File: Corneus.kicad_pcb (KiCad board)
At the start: 2 copper layers, 0 parts

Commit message: PCB layout setup
imported JLCPCB design rules from sethhillbrand, set some settings per ai03's guide, about to import everything and start doing layout
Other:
- copper layers 2 -> 4
- net class Default: clearance 0.2 -> 0.254; trace_width 0.25 -> 0.254
- rule pad_to_mask_clearance: 0.05 -> 0
- rule trace_clearance: 0.2 -> 0.254
- rule trace_min: 0.2 -> 0.127
- rule via_min_size: 0.4 -> 0.6
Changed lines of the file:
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@@
 (kicad_pcb (version 20171130) (host pcbnew "(5.1.6)-1")
   (general
-    (thickness 1.6)
+    (thickness 1.6002)
     (drawings 0)
     (tracks 0)
@@
   )
   (layers
-    (0 F.Cu signal)
-    (31 B.Cu signal)
-    (32 B.Adhes user)
-    (33 F.Adhes user)
+    (0 Front signal)
+    (1 In1.Cu signal)
+    (2 In2.Cu signal)
+    (31 Back signal)
     (34 B.Paste user)
     (35 F.Paste user)
@@
     (38 B.Mask user)
     (39 F.Mask user)
-    (40 Dwgs.User user)
-    (41 Cmts.User user)
-    (42 Eco1.User user)
-    (43 Eco2.User user)
     (44 Edge.Cuts user)
     (45 Margin user)
     (46 B.CrtYd user)
     (47 F.CrtYd user)
-    (48 B.Fab user)
     (49 F.Fab user)
   )
   (setup
-    (last_trace_width 0.25)
-    (trace_clearance 0.2)
+    (last_trace_width 0.254)
+    (user_trace_width 0.15)
+    (user_trace_width 0.2)
+    (user_trace_width 0.4)
+    (user_trace_width 0.6)
+    (trace_clearance 0.254)
     (zone_clearance 0.508)
     (zone_45_only no)
-    (trace_min 0.2)
+    (trace_min 0.127)
     (via_size 0.8)
     (via_drill 0.4)
-    (via_min_size 0.4)
+    (via_min_size 0.6)
     (via_min_drill 0.3)
+    (user_via 0.6 0.3)
+    (user_via 0.9 0.4)
     (uvia_size 0.3)
     (uvia_drill 0.1)
@@
     (pad_size 1.524 1.524)
     (pad_drill 0.762)
-    (pad_to_mask_clearance 0.05)
+    (pad_to_mask_clearance 0)
+    (solder_mask_min_width 0.12)
     (aux_axis_origin 0 0)
     (visible_elements FFFFFF7F)
@@
   (net 0 "")
   (net_class Default "This is the default net class."
-    (clearance 0.2)
-    (trace_width 0.25)
+    (clearance 0.254)
+    (trace_width 0.254)
     (via_dia 0.8)
     (via_drill 0.4)

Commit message: imported schematic and vaguely located switches
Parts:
- added C1: 1uF, Capacitor_SMD:C_0805_2012Metric, F.Cu at (124.7, -13.4)
- added C2: 0.1uF, Capacitor_SMD:C_0805_2012Metric, F.Cu at (255.7, -92.4)
- added C3: 0.1uF, Capacitor_SMD:C_0805_2012Metric, F.Cu at (260.1, -95.4)
- added C4: 0.1uF, Capacitor_SMD:C_0805_2012Metric, F.Cu at (180.3, -14.6)
- added C5: 10uF, Capacitor_SMD:C_0805_2012Metric, F.Cu at (215.3, -43.6)
- added C6: 22pF, Capacitor_SMD:C_0805_2012Metric, F.Cu at (175.9, -14.2)
- added C7: 22pF, Capacitor_SMD:C_0805_2012Metric, F.Cu at (260.1, -92.4)
- added D1: SOD-123, Diode_SMD:D_SOD-123, F.Cu at (144.1, -23.2)
- added D10: SOD-123, Diode_SMD:D_SOD-123, F.Cu at (132.6, -19.9)
- added D11: SOD-123, Diode_SMD:D_SOD-123, F.Cu at (138.3, -23.2)
- added D12: SOD-123, Diode_SMD:D_SOD-123, F.Cu at (98.1, -16.9)
- added D13: SOD-123, Diode_SMD:D_SOD-123, F.Cu at (155.6, -16.5)
- added D14: SOD-123, Diode_SMD:D_SOD-123, F.Cu at (109.6, -16.5)
- added D15: SOD-123, Diode_SMD:D_SOD-123, F.Cu at (115.3, -23.2)
- added D16: SOD-123, Diode_SMD:D_SOD-123, F.Cu at (97.6, -13.5)
- added D17: SOD-123, Diode_SMD:D_SOD-123, F.Cu at (103.8, -16.5)
- added D18: SOD-123, Diode_SMD:D_SOD-123, F.Cu at (109.6, -19.9)
- added D19: SOD-123, Diode_SMD:D_SOD-123, F.Cu at (109.6, -23.2)
- added D2: SOD-123, Diode_SMD:D_SOD-123, F.Cu at (149.8, -23.2)
- added D20: SOD-123, Diode_SMD:D_SOD-123, F.Cu at (103.8, -19.9)
- added D21: SOD-123, Diode_SMD:D_SOD-123, F.Cu at (144.1, -19.9)
- added D22: SOD-123, Diode_SMD:D_SOD-123, F.Cu at (92.3, -16.9)
- added D23: SOD-123, Diode_SMD:D_SOD-123, F.Cu at (86.1, -13.5)
- added D24: SOD-123, Diode_SMD:D_SOD-123, F.Cu at (101.9, -23.2)
- added D25: SOD-123, Diode_SMD:D_SOD-123, F.Cu at (74.6, -15.0)
- added D26: SOD-123, Diode_SMD:D_SOD-123, F.Cu at (115.3, -19.9)
- added D27: SOD-123, Diode_SMD:D_SOD-123, F.Cu at (80.4, -13.5)
- added D28: SOD-123, Diode_SMD:D_SOD-123, F.Cu at (126.8, -23.2)
- added D29: SOD-123, Diode_SMD:D_SOD-123, F.Cu at (132.6, -23.2)
- added D3: SOD-123, Diode_SMD:D_SOD-123, F.Cu at (121.1, -19.9)
- added D30: SOD-123, Diode_SMD:D_SOD-123, F.Cu at (121.1, -23.2)
- added D31: SOD-123, Diode_SMD:D_SOD-123, F.Cu at (161.3, -19.9)
- added D32: SOD-123, Diode_SMD:D_SOD-123, F.Cu at (172.8, -23.2)
- added D33: SOD-123, Diode_SMD:D_SOD-123, F.Cu at (167.1, -23.2)
- added D34: SOD-123, Diode_SMD:D_SOD-123, F.Cu at (161.3, -23.2)
- added D35: SOD-123, Diode_SMD:D_SOD-123, F.Cu at (155.6, -19.9)
- added D36: SOD-123, Diode_SMD:D_SOD-123, F.Cu at (149.8, -16.5)
- added D37: SOD-123, Diode_SMD:D_SOD-123, F.Cu at (155.6, -23.2)
- added D38: SOD-123, Diode_SMD:D_SOD-123, F.Cu at (144.1, -16.5)
- added D39: SOD-123, Diode_SMD:D_SOD-123, F.Cu at (167.1, -19.9)
- added D4: SOD-123, Diode_SMD:D_SOD-123, F.Cu at (126.8, -16.5)
- added D40: SOD-123, Diode_SMD:D_SOD-123, F.Cu at (138.3, -16.5)
- added D41: SOD-123, Diode_SMD:D_SOD-123, F.Cu at (132.6, -16.5)
- added D42: SOD-123, Diode_SMD:D_SOD-123, F.Cu at (149.8, -19.9)
- added D5: SOD-123, Diode_SMD:D_SOD-123, F.Cu at (121.1, -16.5)
- added D6: SOD-123, Diode_SMD:D_SOD-123, F.Cu at (126.8, -19.9)
- added D7: SOD-123, Diode_SMD:D_SOD-123, F.Cu at (91.9, -13.5)
- added D8: SOD-123, Diode_SMD:D_SOD-123, F.Cu at (115.3, -16.5)
- added D9: SOD-123, Diode_SMD:D_SOD-123, F.Cu at (138.3, -19.9)
- added F1: 500mA, Fuse:Fuse_1206_3216Metric, F.Cu at (161.3, -16.6)
- added J1: USB_B_Micro, Choco617_parts:CUI_UJ2-MIBH2-4-SMT, F.Cu at (87.0, -21.3)
- added MX1: MX-LED, Choco617_parts:Kailh_socket_MX_PCBmount_LED_1U, F.Cu at (25.4, 30.2)
- added MX10: MX-LED, Choco617_parts:Kailh_socket_MX_PCBmount_LED_1U, F.Cu at (200.8, 30.2)
- added MX11: MX-LED, Choco617_parts:Kailh_socket_MX_PCBmount_LED_1U, F.Cu at (218.3, 30.2)
- added MX12: MX-LED, Choco617_parts:Kailh_socket_MX_PCBmount_LED_1U, F.Cu at (236.5, 30.2)
- added MX13: MX-LED, Choco617_parts:Kailh_socket_MX_PCBmount_LED_1U, F.Cu at (25.4, 48.4)
- added MX14: MX-LED, Choco617_parts:Kailh_socket_MX_PCBmount_LED_1U, F.Cu at (43.7, 47.6)
- added MX15: MX-LED, Choco617_parts:Kailh_socket_MX_PCBmount_LED_1U, F.Cu at (61.9, 47.6)
- added MX16: MX-LED, Choco617_parts:Kailh_socket_MX_PCBmount_LED_1U, F.Cu at (81.0, 47.6)
- added MX17: MX-LED, Choco617_parts:Kailh_socket_MX_PCBmount_LED_1U, F.Cu at (99.2, 47.6)
- added MX18: MX-LED, Choco617_parts:Kailh_socket_MX_PCBmount_LED_1U, F.Cu at (116.7, 47.6)
- added MX19: MX-LED, Choco617_parts:Kailh_socket_MX_PCBmount_LED_1U, F.Cu at (146.8, 49.2)
- added MX2: MX-LED, Choco617_parts:Kailh_socket_MX_PCBmount_LED_1U, F.Cu at (43.7, 30.2)
- added MX20: MX-LED, Choco617_parts:Kailh_socket_MX_PCBmount_LED_1U, F.Cu at (166.7, 49.2)
- added MX21: MX-LED, Choco617_parts:Kailh_socket_MX_PCBmount_LED_1U, F.Cu at (182.6, 49.2)
- added MX22: MX-LED, Choco617_parts:Kailh_socket_MX_PCBmount_LED_1U, F.Cu at (200.8, 49.2)
- added MX23: MX-LED, Choco617_parts:Kailh_socket_MX_PCBmount_LED_1U, F.Cu at (219.1, 49.2)
- added MX24: MX-LED, Choco617_parts:Kailh_socket_MX_PCBmount_LED_1U, F.Cu at (236.5, 49.2)
- added MX25: MX-LED, Choco617_parts:Kailh_socket_MX_PCBmount_LED_1U, F.Cu at (24.6, 65.1)
- added MX26: MX-LED, Choco617_parts:Kailh_socket_MX_PCBmount_LED_1U, F.Cu at (42.9, 65.1)
- added MX27: MX-LED, Choco617_parts:Kailh_socket_MX_PCBmount_LED_1U, F.Cu at (61.1, 65.9)
- added MX28: MX-LED, Choco617_parts:Kailh_socket_MX_PCBmount_LED_1U, F.Cu at (81.0, 65.1)
- added MX29: MX-LED, Choco617_parts:Kailh_socket_MX_PCBmount_LED_1U, F.Cu at (99.2, 65.9)
- added MX3: MX-LED, Choco617_parts:Kailh_socket_MX_PCBmount_LED_1U, F.Cu at (61.9, 30.2)
- added MX30: MX-LED, Choco617_parts:Kailh_socket_MX_PCBmount_LED_1U, F.Cu at (116.7, 65.1)
- added MX31: MX-LED, Choco617_parts:Kailh_socket_MX_PCBmount_LED_1U, F.Cu at (146.8, 65.9)
- added MX32: MX-LED, Choco617_parts:Kailh_socket_MX_PCBmount_LED_1U, F.Cu at (166.7, 65.9)
- added MX33: MX-LED, Choco617_parts:Kailh_socket_MX_PCBmount_LED_1U, F.Cu at (183.4, 66.7)
- added MX34: MX-LED, Choco617_parts:Kailh_socket_MX_PCBmount_LED_1U, F.Cu at (200.8, 67.5)
- added MX35: MX-LED, Choco617_parts:Kailh_socket_MX_PCBmount_LED_1U, F.Cu at (219.1, 68.3)
- added MX36: MX-LED, Choco617_parts:Kailh_socket_MX_PCBmount_LED_1U, F.Cu at (236.5, 67.5)
- added MX37: MX-LED, Choco617_parts:Kailh_socket_MX_PCBmount_LED_1U, F.Cu at (81.0, 84.9)
- added MX38: MX-LED, Choco617_parts:Kailh_socket_MX_PCBmount_LED_1U, F.Cu at (99.2, 84.9)
- added MX39: MX-LED, Choco617_parts:Kailh_socket_MX_PCBmount_LED_1U, F.Cu at (116.7, 84.9)
- added MX4: MX-LED, Choco617_parts:Kailh_socket_MX_PCBmount_LED_1U, F.Cu at (81.0, 30.2)
- added MX40: MX-LED, Choco617_parts:Kailh_socket_MX_PCBmount_LED_1U, F.Cu at (146.1, 85.7)
- added MX41: MX-LED, Choco617_parts:Kailh_socket_MX_PCBmount_LED_1U, F.Cu at (165.9, 85.7)
- added MX42: MX-LED, Choco617_parts:Kailh_socket_MX_PCBmount_LED_1U, F.Cu at (184.2, 85.7)
- added MX5: MX-LED, Choco617_parts:Kailh_socket_MX_PCBmount_LED_1U, F.Cu at (99.2, 30.2)
- added MX6: MX-LED, Choco617_parts:Kailh_socket_MX_PCBmount_LED_1U, F.Cu at (116.7, 30.2)
- added MX7: MX-LED, Choco617_parts:Kailh_socket_MX_PCBmount_LED_1U, F.Cu at (147.6, 30.2)
- added MX8: MX-LED, Choco617_parts:Kailh_socket_MX_PCBmount_LED_1U, F.Cu at (165.9, 30.2)
- added MX9: MX-LED, Choco617_parts:Kailh_socket_MX_PCBmount_LED_1U, F.Cu at (182.6, 30.2)
- added NPNR1: 1.5k, Resistor_SMD:R_0805_2012Metric, F.Cu at (111.5, -13.4)
- added Q1: Q_NPN_BCE, Package_TO_SOT_SMD:SOT-223, F.Cu at (76.7, -20.8)
- added R1: 470, Resistor_SMD:R_0805_2012Metric, F.Cu at (177.9, -23.4)
- added R10: 470, Resistor_SMD:R_0805_2012Metric, F.Cu at (102.7, -13.4)
- added R11: 470, Resistor_SMD:R_0805_2012Metric, F.Cu at (133.6, -13.4)
- added R12: 470, Resistor_SMD:R_0805_2012Metric, F.Cu at (129.1, -13.4)
- added R13: 470, Resistor_SMD:R_0805_2012Metric, F.Cu at (120.3, -13.4)
- added R14: 470, Resistor_SMD:R_0805_2012Metric, F.Cu at (115.9, -13.4)
- added R15: 470, Resistor_SMD:R_0805_2012Metric, F.Cu at (260.1, -98.3)
- added R16: 470, Resistor_SMD:R_0805_2012Metric, F.Cu at (171.5, -16.7)
- added R17: 470, Resistor_SMD:R_0805_2012Metric, F.Cu at (255.7, -101.3)
- added R18: 470, Resistor_SMD:R_0805_2012Metric, F.Cu at (264.6, -104.2)
- added R19: 470, Resistor_SMD:R_0805_2012Metric, F.Cu at (235.5, -66.6)
- added R2: 470, Resistor_SMD:R_0805_2012Metric, F.Cu at (138.0, -13.4)
- added R20: 470, Resistor_SMD:R_0805_2012Metric, F.Cu at (184.8, -14.6)
- added R21: 470, Resistor_SMD:R_0805_2012Metric, F.Cu at (264.6, -95.4)
- added R22: 470, Resistor_SMD:R_0805_2012Metric, F.Cu at (255.7, -86.5)
- added R23: 470, Resistor_SMD:R_0805_2012Metric, F.Cu at (189.8, -20.5)
- added R24: 470, Resistor_SMD:R_0805_2012Metric, F.Cu at (172.2, -20.1)
- added R25: 470, Resistor_SMD:R_0805_2012Metric, F.Cu at (239.9, -69.6)
- added R26: 470, Resistor_SMD:R_0805_2012Metric, F.Cu at (191.1, -23.4)
- added R27: 470, Resistor_SMD:R_0805_2012Metric, F.Cu at (185.4, -17.5)
- added R28: 470, Resistor_SMD:R_0805_2012Metric, F.Cu at (255.7, -95.4)
- added R29: 470, Resistor_SMD:R_0805_2012Metric, F.Cu at (185.4, -20.5)
- added R3: 470, Resistor_SMD:R_0805_2012Metric, F.Cu at (255.7, -104.2)
- added R30: 470, Resistor_SMD:R_0805_2012Metric, F.Cu at (255.7, -89.5)
- added R31: 470, Resistor_SMD:R_0805_2012Metric, F.Cu at (269.0, -101.3)
- added R32: 470, Resistor_SMD:R_0805_2012Metric, F.Cu at (264.6, -98.3)
- added R33: 470, Resistor_SMD:R_0805_2012Metric, F.Cu at (260.1, -101.3)
- added R34: 470, Resistor_SMD:R_0805_2012Metric, F.Cu at (181.0, -17.5)
- added R35: 470, Resistor_SMD:R_0805_2012Metric, F.Cu at (269.0, -104.2)
- added R36: 470, Resistor_SMD:R_0805_2012Metric, F.Cu at (181.0, -20.5)
- added R37: 470, Resistor_SMD:R_0805_2012Metric, F.Cu at (186.7, -23.4)
- added R38: 470, Resistor_SMD:R_0805_2012Metric, F.Cu at (235.5, -69.6)
- added R39: 470, Resistor_SMD:R_0805_2012Metric, F.Cu at (182.3, -23.4)
- added R4: 470, Resistor_SMD:R_0805_2012Metric, F.Cu at (160.0, -13.4)
- added R40: 470, Resistor_SMD:R_0805_2012Metric, F.Cu at (260.1, -104.2)
- added R41: 470, Resistor_SMD:R_0805_2012Metric, F.Cu at (255.7, -98.3)
- added R42: 470, Resistor_SMD:R_0805_2012Metric, F.Cu at (264.6, -101.3)
- added R43: 10k, Resistor_SMD:R_0805_2012Metric, F.Cu at (171.5, -13.8)
- added R44: 22, Resistor_SMD:R_0805_2012Metric, F.Cu at (175.9, -17.1)
- added R45: 22, Resistor_SMD:R_0805_2012Metric, F.Cu at (176.6, -20.1)
- added R46: 10k, Resistor_SMD:R_0805_2012Metric, F.Cu at (250.0, -84.0)
- added R5: 470, Resistor_SMD:R_0805_2012Metric, F.Cu at (155.6, -13.4)
- added R6: 470, Resistor_SMD:R_0805_2012Metric, F.Cu at (107.1, -13.4)
- added R7: 470, Resistor_SMD:R_0805_2012Metric, F.Cu at (151.2, -13.4)
- added R8: 470, Resistor_SMD:R_0805_2012Metric, F.Cu at (146.8, -13.4)
- added R9: 470, Resistor_SMD:R_0805_2012Metric, F.Cu at (142.4, -13.4)
- added SW1: SW_Push, random-keyboard-parts:SKQG-1155865, F.Cu at (94.2, -21.7)
- added U1: ATmega32U4-AU, Package_QFP:TQFP-44_10x10mm_P0.8mm, F.Cu at (240.6, -78.3)
- added U2: PRTR5V0U2X, random-keyboard-parts:SOT143B, F.Cu at (249.8, -80.5)
- added Y1: 16MHz, Crystal:Crystal_SMD_3225-4Pin_3.2x2.5mm, F.Cu at (166.7, -16.0)
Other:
- board outline added: 0.8 x 5.1 mm

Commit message: vaguely located MCU related components
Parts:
- moved C3 206.7 mm to (143.7, 75.4), turned to 180 degrees
- moved C7 206.2 mm to (131.0, 68.3)
- moved C2 189.5 mm to (158.0, 69.8), turned to 90 degrees
- moved R46 186.5 mm to (153.2, 75.4), turned to 180 degrees
- moved U1 171.1 mm to (148.4, 65.9), turned to 270 degrees
- moved U2 146.1 mm to (150.0, 26.2), turned to 90 degrees
- moved Q1 131.7 mm to (148.4, 89.7)
- moved C5 118.1 mm to (156.4, 58.7), turned to 270 degrees
- moved R21 96.5 mm to (211.1, -15.1)
- moved R32 94.9 mm to (211.1, -19.8)
- moved R15 94.7 mm to (207.2, -19.8)
- moved R41 94.5 mm to (203.2, -19.8)
- moved R31 93.3 mm to (215.1, -25.1)
- moved R42 93.1 mm to (211.1, -25.1)
- moved R33 92.8 mm to (207.2, -25.1)
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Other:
- board size 0.8 x 5.1 mm -> 5.1 x 0.8 mm

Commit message: precisely located all switches
switches, diodes, and LED resistors located by coordinates generated from mechanical CAD layout
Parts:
- moved R25 215.4 mm to (37.6, 107.0), turned to 75 degrees
- moved NPNR1 214.1 mm to (31.7, 185.3), turned to 180 degrees
- moved D24 197.9 mm to (271.4, 78.9), turned to 105 degrees
- moved D23 193.2 mm to (253.0, 83.8), turned to 105 degrees
- moved R26 191.3 mm to (56.0, 111.9), turned to 75 degrees
- moved R39 188.0 mm to (131.4, 157.5), turned to 45 degrees
- moved D12 185.3 mm to (266.4, 60.6), turned to 105 degrees
- moved R37 178.5 mm to (99.7, 132.4), turned to 75 degrees
- moved R40 176.2 mm to (178.6, 143.7), turned to 135 degrees
- moved D39 175.4 mm to (136.2, 152.8), turned to 45 degrees
- moved R38 175.1 mm to (117.6, 142.5), turned to 60 degrees
- moved R28 171.2 mm to (97.4, 104.4), turned to 75 degrees
- moved D36 170.1 mm to (276.3, 97.3), turned to 105 degrees
- moved D22 168.0 mm to (231.5, 77.2), turned to 105 degrees
- moved R15 164.2 mm to (82.4, 86.9), turned to 75 degrees
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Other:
- outline, holes or cut-outs redrawn

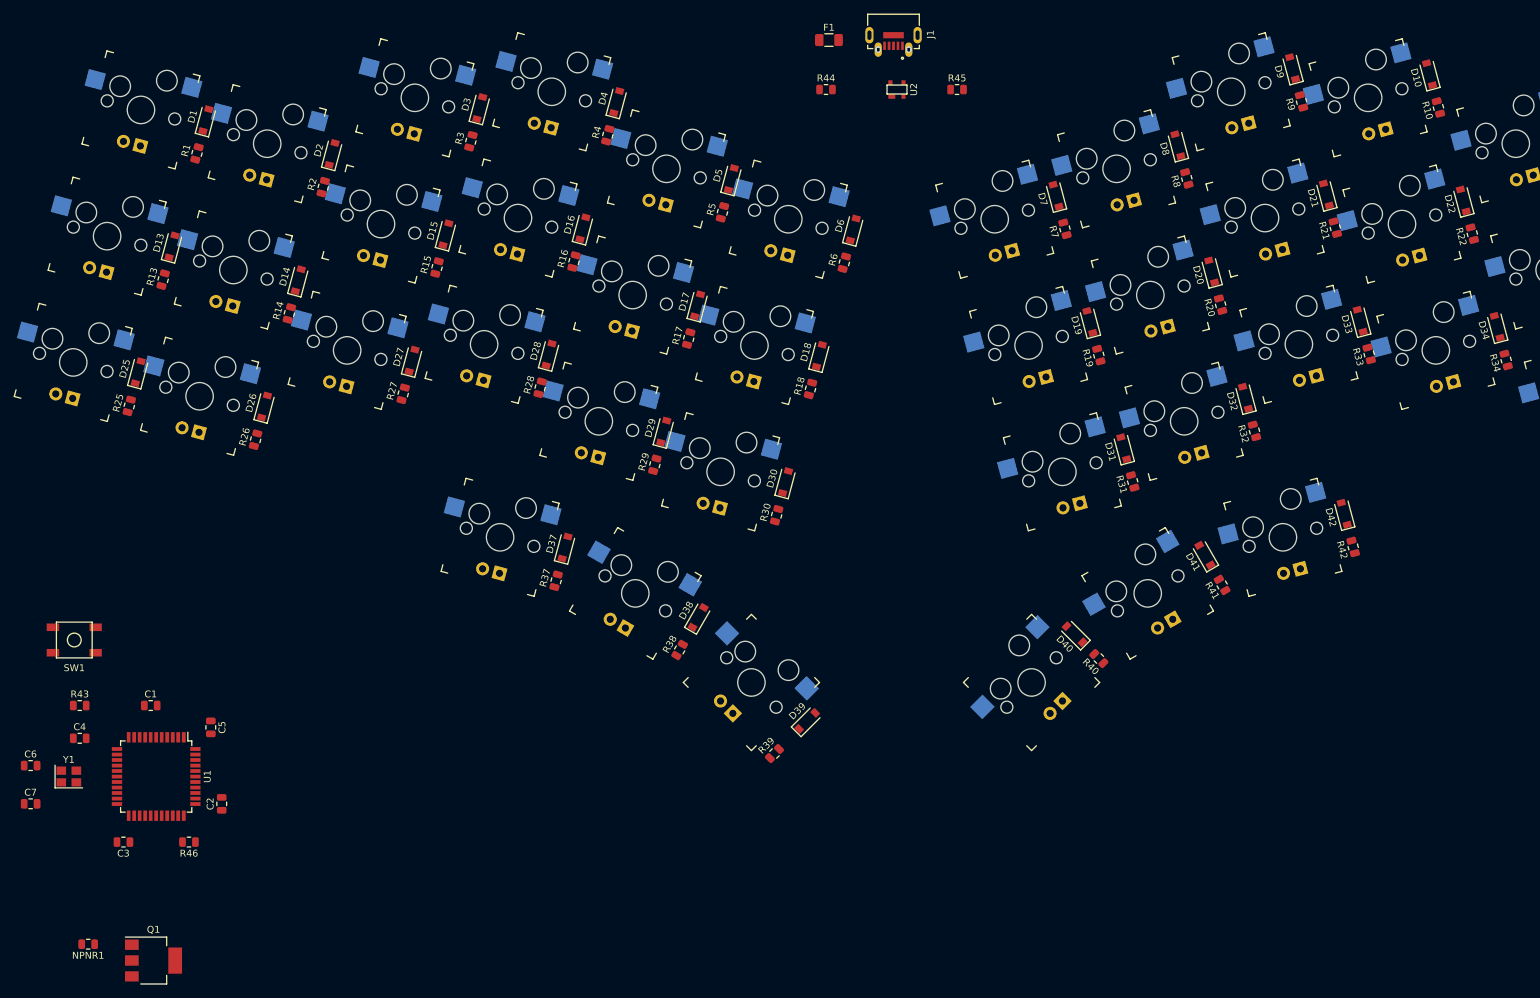
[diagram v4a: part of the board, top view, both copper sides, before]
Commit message: MCU components better placed
moved MCU components around atmega32u4 as needed, moved whole group to center, moved MOSFET to right hand gap under period, moved reset switch to left hand under X
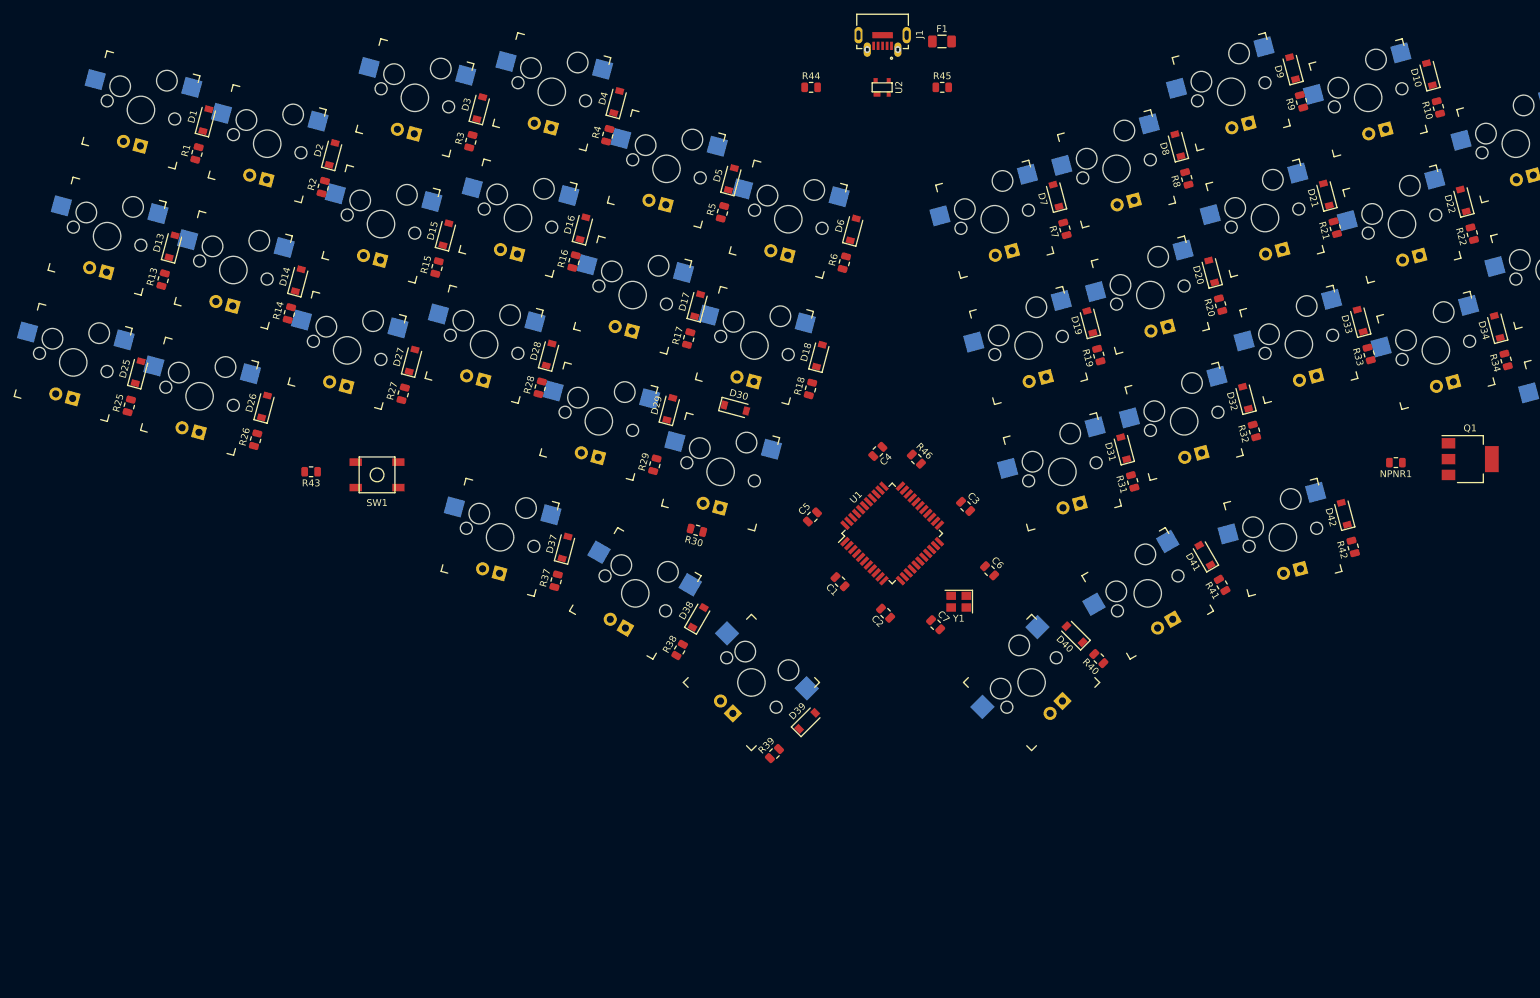
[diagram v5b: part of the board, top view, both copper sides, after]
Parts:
- moved Q1 204.8 mm to (232.5, 114.7)
- moved NPNR1 202.6 mm to (221.7, 115.3)
- moved C6 142.2 mm to (162.7, 131.0), turned to 315 degrees
- moved C7 134.1 mm to (154.8, 138.8), turned to 315 degrees
- moved Y1 131.8 mm to (158.2, 135.5), turned to 180 degrees
- moved C3 131.8 mm to (159.2, 121.6), turned to 315 degrees
- moved C4 123.3 mm to (146.4, 113.6), turned to 225 degrees
- moved R46 119.5 mm to (152.0, 114.8), turned to 315 degrees
- moved U1 112.7 mm to (148.5, 125.5), turned to 45 degrees
- moved C1 101.8 mm to (141.0, 132.6), turned to 135 degrees
- moved C2 100.4 mm to (147.6, 137.1), turned to 135 degrees
- moved C5 92.6 mm to (136.9, 123.1), turned to 45 degrees
- moved SW1 50.1 mm to (73.7, 117.0)
- moved R43 47.8 mm to (64.1, 116.6), turned to 180 degrees
- moved F1 16.4 mm to (155.8, 54.0)
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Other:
- outline, holes or cut-outs redrawn

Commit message: added edge cuts
-corrected layer settings
-made net class settings
-added edge cuts
-located MCU components pretty precisely
-located micro USB precisely
-started routing
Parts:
- moved R44 2.26 mm to (138.9, 59.9)
- moved J1 1.89 mm to (149.7, 53.3)
- moved R45 1.65 mm to (157.3, 59.9), turned to 180 degrees
- moved U2 1.65 mm to (148.5, 59.9)
- moved R46 1.55 mm to (151.0, 113.6)
- moved F1 1.49 mm to (157.2, 53.5), turned to 180 degrees
- moved C1 1.09 mm to (140.2, 133.4)
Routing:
- net +5V: track 0.00 -> 24.4 mm
- net Net-(C6-Pad1): track 0.00 -> 14.2 mm
- net Net-(C7-Pad1): track 0.00 -> 12.6 mm
- net GND: track 0.00 -> 10.1 mm
- net Net-(C1-Pad1): track 0.00 -> 5.96 mm
- net Net-(R46-Pad2): track 0.00 -> 5.22 mm
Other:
- board size 5.1 x 0.8 mm -> 262 x 112 mm
- copper layers 4 -> 2
- net class Power added: clearance 0.254, trace_width 0.381, via_dia 0.8, via_drill 0.4

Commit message: more MCU routing
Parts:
- moved R45 15.8 mm to (141.5, 60.8), turned to 90 degrees
- moved R44 15.8 mm to (154.6, 60.9), turned to 90 degrees
- turned SW1 to 180 degrees
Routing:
- net +5V: track 24.4 -> 131.0 mm
- net Net-(R43-Pad2): track 0.00 -> 94.6 mm, vias 0 -> 2
- net D+: track 0.00 -> 83.9 mm
- net D-: track 0.00 -> 81.5 mm, vias 0 -> 2
- net Net-(J1-Pad3): track 0.00 -> 15.3 mm, vias 0 -> 2
- net Net-(J1-Pad2): track 0.00 -> 14.8 mm
- net GND: track 10.1 -> 1.59 mm
- net Net-(NPNR1-Pad1): track 0.00 -> 7.87 mm
- net Net-(C6-Pad1): track 14.2 -> 13.5 mm

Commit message: routed all switches to their diodes
also some column 0 stuff
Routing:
- net +5V: track 131.0 -> 189.7 mm
- net COL0: track 0.00 -> 40.8 mm
- net ROW0: track 0.00 -> 20.4 mm
- net Net-(D30-Pad2): track 0.00 -> 9.20 mm, vias 0 -> 1
- net Net-(MX1-Pad4): track 0.00 -> 8.81 mm
- net Net-(D42-Pad2): track 0.00 -> 7.58 mm, vias 0 -> 1
- net Net-(D22-Pad2): track 0.00 -> 6.88 mm, vias 0 -> 1
- net Net-(D21-Pad2): track 0.00 -> 6.71 mm, vias 0 -> 1
- net Net-(D36-Pad2): track 0.00 -> 6.67 mm, vias 0 -> 1
- net Net-(D32-Pad2): track 0.00 -> 6.58 mm, vias 0 -> 1
- net Net-(D20-Pad2): track 0.00 -> 6.56 mm, vias 0 -> 1
- net Net-(D39-Pad2): track 0.00 -> 6.56 mm, vias 0 -> 1
- net Net-(D9-Pad2): track 0.00 -> 6.55 mm, vias 0 -> 1
- net Net-(D35-Pad2): track 0.00 -> 6.44 mm, vias 0 -> 1
- net Net-(D29-Pad2): track 0.00 -> 6.41 mm, vias 0 -> 1
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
